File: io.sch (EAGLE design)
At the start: 34 parts, among them J1 SJ-3523-SMT-TR, Q1 MMBT2222A-7-FSOT-23_DIO-M, Q2 2SCR574D3TL1TRANS_2SCR573_TO-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, U1 MCP1703T-5002E, U3 LM386M-1

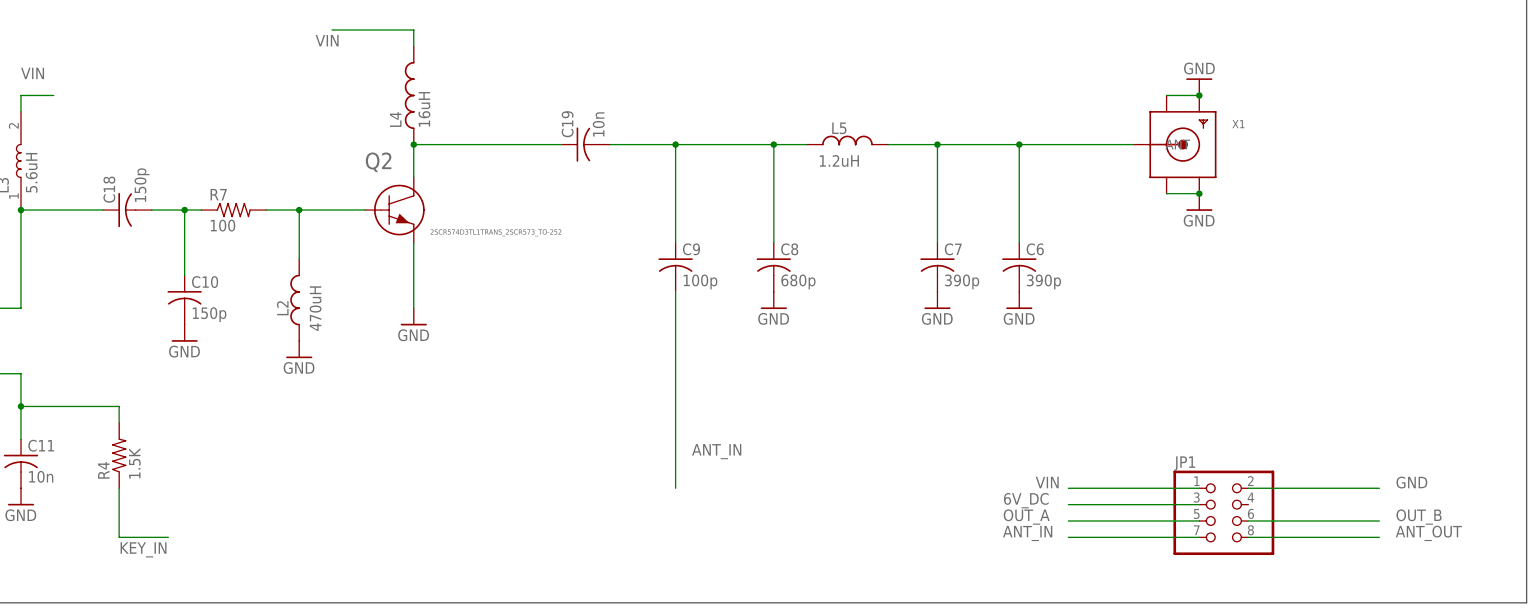
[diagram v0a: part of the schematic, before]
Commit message: v1.2 boards
* corrected C22 as a 33uF (vs 33pF) capacitor with a 1206 footprint
* Q2 emitter is now tied to Q1 emitter and KEY_IN to cut down on self resonance
* Unused pin 4 on JP1 now tied to GND
* All pins on JP1 labelled on top and bottom of each board
* lots more GND vias
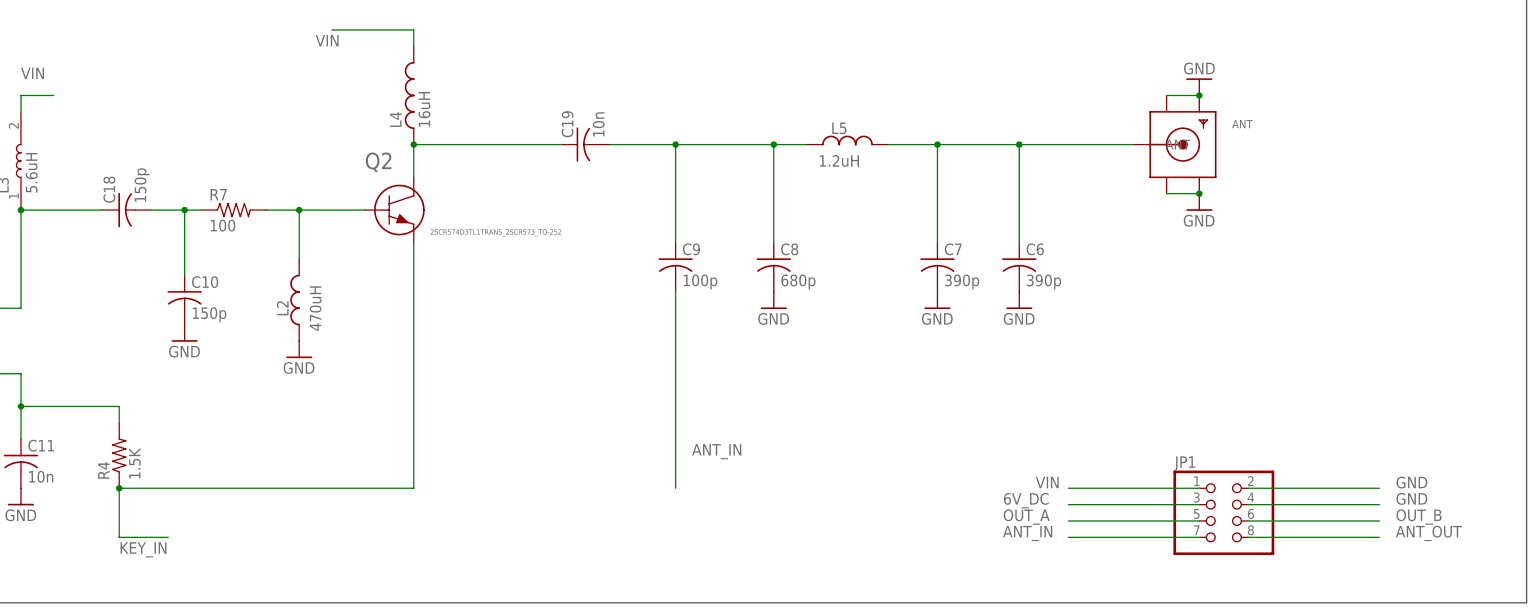
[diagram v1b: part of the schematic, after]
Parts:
- C22: device adafruit:C-USC0805 -> adafruit:C-USC1206
- renumbered X1 to ANT
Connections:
- net GND: now also JP1.4; no longer Q2.3
- net KEY_IN: now also Q2.3
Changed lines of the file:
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@@
 </classes>
 <parts>
-<part name="C22" library="adafruit" library_urn="urn:adsk.eagle:library:420" deviceset="C-US" device="C0805" package3d_urn="urn:adsk.eagle:package:6240337/1" value="33U"/>
+<part name="C22" library="adafruit" library_urn="urn:adsk.eagle:library:420" deviceset="C-US" device="C1206" package3d_urn="urn:adsk.eagle:package:6240335/1" value="33U"/>
 <part name="C1" library="adafruit" library_urn="urn:adsk.eagle:library:420" deviceset="C-US" device="C0805" package3d_urn="urn:adsk.eagle:package:6240337/1" value="0.1U"/>
 <part name="C2" library="adafruit" library_urn="urn:adsk.eagle:library:420" deviceset="C-US" device="C0805" package3d_urn="urn:adsk.eagle:package:6240337/1" value="10n"/>
@@
 <part name="R7" library="adafruit" library_urn="urn:adsk.eagle:library:420" deviceset="R-US_" device="M0805" package3d_urn="urn:adsk.eagle:package:6240587/1" value="100"/>
 <part name="GND21" library="supply1" library_urn="urn:adsk.eagle:library:371" deviceset="GND" device=""/>
-<part name="GND22" library="supply1" library_urn="urn:adsk.eagle:library:371" deviceset="GND" device=""/>
 <part name="GND23" library="supply1" library_urn="urn:adsk.eagle:library:371" deviceset="GND" device=""/>
 <part name="GND24" library="supply1" library_urn="urn:adsk.eagle:library:371" deviceset="GND" device=""/>
@@
 <part name="L2" library="zort2" deviceset="L" device="CHIP-1008(2520-METRIC)" package3d_urn="urn:adsk.eagle:package:16378469/1" technology="_" value="470uH"/>
 <part name="J1" library="SJ-3523-SMT-TR" deviceset="SJ-3523-SMT-TR" device=""/>
-<part name="X1" library="zort2" deviceset="SMACONNECTOR" device="_EDGE" package3d_urn="urn:adsk.eagle:package:6240945/1"/>
+<part name="ANT" library="zort2" deviceset="SMACONNECTOR" device="_EDGE" package3d_urn="urn:adsk.eagle:package:6240945/1"/>
 <part name="Q1" library="zort2" deviceset="MMBT2222A-7-F" device="SOT-23_DIO-M"/>
 </parts>
@@
 <attribute name="VALUE" x="22.86" y="-25.4" size="1.778" layer="96"/>
 </instance>
-<instance part="GND22" gate="1" x="43.18" y="-17.78" smashed="yes">
-<attribute name="VALUE" x="40.64" y="-20.32" size="1.778" layer="96"/>
-</instance>
 <instance part="GND23" gate="1" x="165.1" y="0" smashed="yes">
 <attribute name="VALUE" x="162.56" y="-2.54" size="1.778" layer="96"/>
@@
 <attribute name="NAME" x="185.440409375" y="73.002040625" size="2.201440625" layer="95" rot="R180"/>
 </instance>
-<instance part="X1" gate="G$1" x="162.56" y="10.16" smashed="yes">
+<instance part="ANT" gate="G$1" x="162.56" y="10.16" smashed="yes">
 <attribute name="NAME" x="170.18" y="12.7" size="1.27" layer="95"/>
 <attribute name="VALUE" x="170.18" y="10.16" size="1.27" layer="95"/>
@@
 </segment>
 <segment>
-<pinref part="GND22" gate="1" pin="GND"/>
-<wire x1="43.18" y1="-5.08" x2="43.18" y2="-15.24" width="0.1524" layer="91"/>
-<pinref part="Q2" gate="A" pin="3"/>
-</segment>
-<segment>
 <pinref part="GND23" gate="1" pin="GND"/>
-<pinref part="X1" gate="G$1" pin="GND4"/>
+<pinref part="ANT" gate="G$1" pin="GND4"/>
 <junction x="165.1" y="2.54"/>
 </segment>
 <segment>
 <pinref part="GND24" gate="1" pin="GND"/>
-<pinref part="X1" gate="G$1" pin="GND2"/>
+<pinref part="ANT" gate="G$1" pin="GND2"/>
 <junction x="165.1" y="17.78"/>
 </segment>
@@
 <pinref part="GND21" gate="1" pin="GND"/>
 <pinref part="L2" gate="G$1" pin="1"/>
+</segment>
+<segment>
+<pinref part="JP1" gate="A" pin="4"/>
+<wire x1="172.72" y1="-45.72" x2="193.04" y2="-45.72" width="0.1524" layer="91"/>
+<label x="195.58" y="-45.72" size="1.778" layer="95"/>
 </segment>
 </net>
@@
 </segment>
 </net>
-<net name="KEY_IN" class="0">
+<net name="KEY_IN" class="1">
 <segment>
 <label x="154.94" y="73.66" size="1.778" layer="95" rot="R270"/>
@@
 <label x="-2.54" y="-53.34" size="1.778" layer="95"/>
 <wire x1="-2.54" y1="-50.8" x2="5.08" y2="-50.8" width="0.1524" layer="91"/>
+<pinref part="Q2" gate="A" pin="3"/>
+<wire x1="-2.54" y1="-43.18" x2="43.18" y2="-43.18" width="0.1524" layer="91"/>
+<wire x1="43.18" y1="-43.18" x2="43.18" y2="-5.08" width="0.1524" layer="91"/>
+<junction x="-2.54" y="-43.18"/>
 </segment>
 </net>
@@
 </segment>
 </net>
-<net name="N$19" class="0">
+<net name="N$19" class="1">
 <segment>
 <pinref part="C12" gate="G$1" pin="2"/>
@@
 </segment>
 </net>
-<net name="N$20" class="0">
+<net name="N$20" class="1">
 <segment>
 <pinref part="C11" gate="G$1" pin="1"/>
@@
 <junction x="137.16" y="10.16"/>
 <pinref part="L5" gate="G$1" pin="2"/>
-<pinref part="X1" gate="G$1" pin="ANT"/>
+<pinref part="ANT" gate="G$1" pin="ANT"/>
 </segment>
 </net>
@@
 <segment>
 <wire x1="160.02" y1="2.54" x2="165.0238" y2="2.54" width="0.1524" layer="91"/>
-<pinref part="X1" gate="G$1" pin="GND3"/>
+<pinref part="ANT" gate="G$1" pin="GND3"/>
 </segment>
 </net>
@@
 <segment>
 <wire x1="160.02" y1="17.78" x2="165.0238" y2="17.78" width="0.1524" layer="91"/>
-<pinref part="X1" gate="G$1" pin="GND1"/>
-</segment>
-</net>
+<pinref part="ANT" gate="G$1" pin="GND1"/>
+</segment>
+</net>

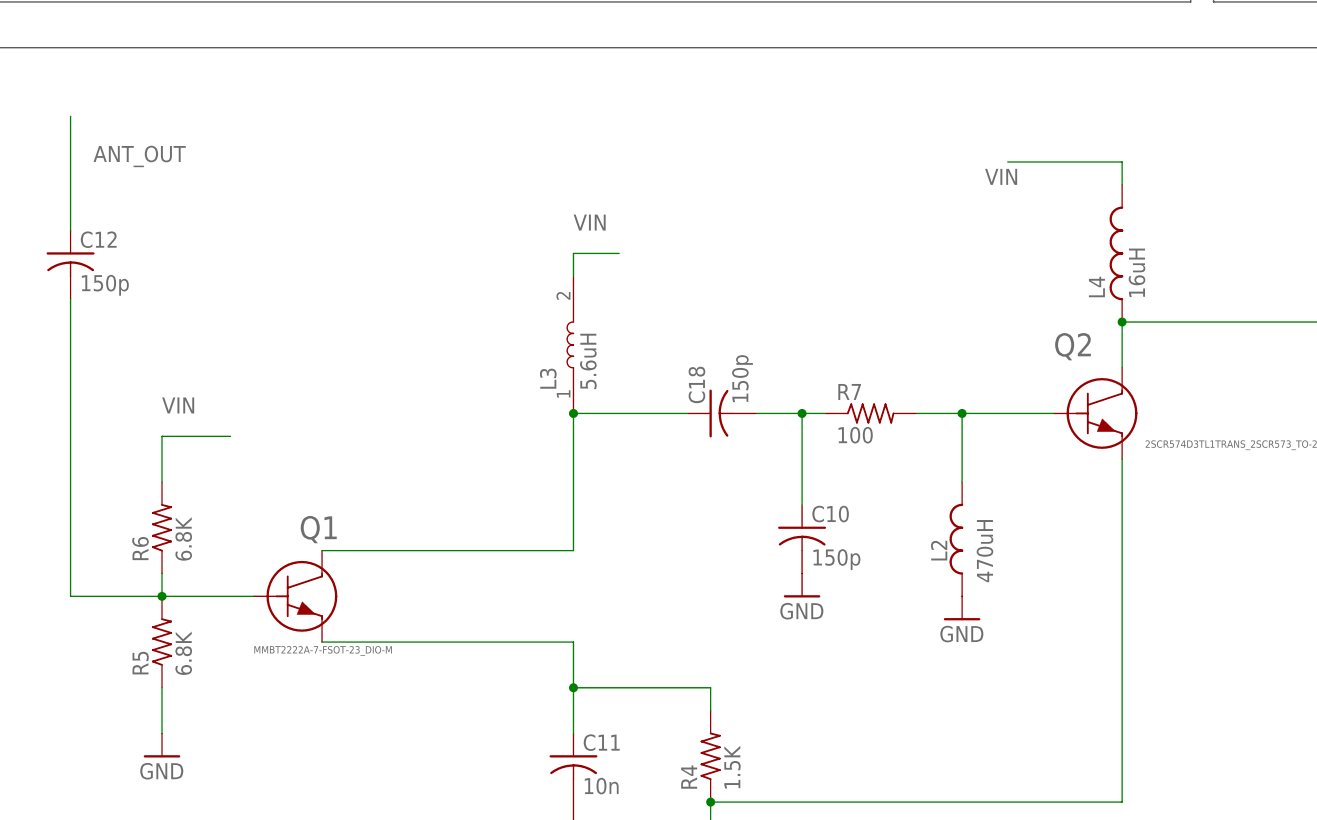
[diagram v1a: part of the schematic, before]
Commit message: v1.2 updated inductors
* updated L3 to a 650mA capable 5.6uH flat package
* updated L4 to a 3A capable 15uH flat package... 16uH are difficult to come by
* general board cleanup for readability
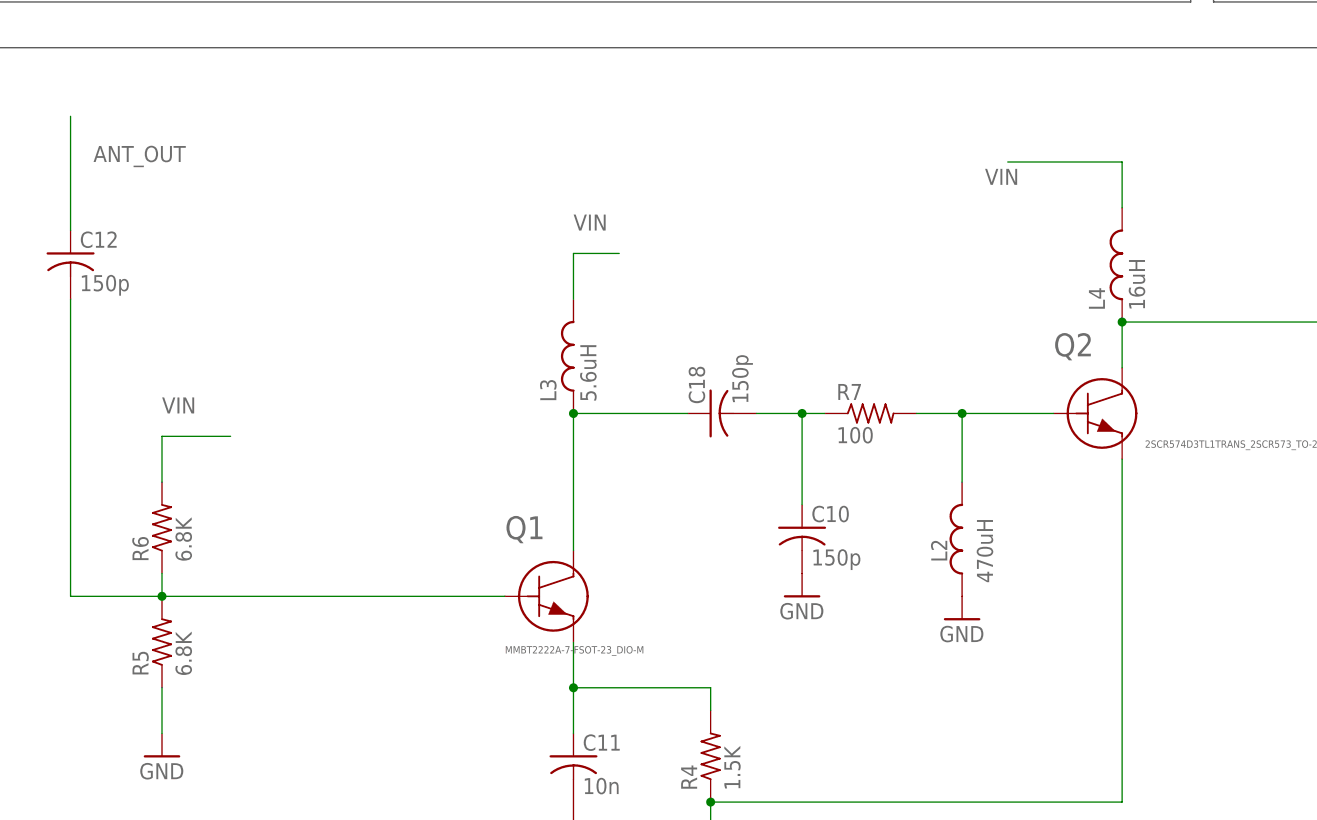
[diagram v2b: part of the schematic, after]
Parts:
- L3: device MLF2012E5R6KT000:MLF2012E5R6KT000 -> zort2:SRP3012C-5R6M
- L4: device LQW18AN16NG8ZD:LQW18AN16NG8ZD -> zort2:ASPI-0630LR
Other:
- moved on the sheet: Q1
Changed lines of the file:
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@@
 <part name="GND19" library="supply1" library_urn="urn:adsk.eagle:library:371" deviceset="GND" device=""/>
 <part name="GND20" library="supply1" library_urn="urn:adsk.eagle:library:371" deviceset="GND" device=""/>
-<part name="L3" library="MLF2012E5R6KT000" deviceset="MLF2012E5R6KT000" device="" value="5.6uH"/>
+<part name="L3" library="zort2" deviceset="SRP3012C-5R6M" device="" value="5.6uH"/>
 <part name="R7" library="adafruit" library_urn="urn:adsk.eagle:library:420" deviceset="R-US_" device="M0805" package3d_urn="urn:adsk.eagle:package:6240587/1" value="100"/>
 <part name="GND21" library="supply1" library_urn="urn:adsk.eagle:library:371" deviceset="GND" device=""/>
@@
 <part name="JP1" library="adafruit" library_urn="urn:adsk.eagle:library:420" deviceset="PINHD-2X4" device="" package3d_urn="urn:adsk.eagle:package:6240893/1"/>
 <part name="L5" library="Inductor" library_urn="urn:adsk.eagle:library:16378440" deviceset="L" device="CHIP-0805(2012-METRIC)" package3d_urn="urn:adsk.eagle:package:16378480/1" technology="_" value="1.2uH"/>
-<part name="L4" library="LQW18AN16NG8ZD" deviceset="LQW18AN16NG8ZD" device="" value="16uH"/>
+<part name="L4" library="zort2" deviceset="ASPI-0630LR" device="" value="16uH"/>
 <part name="U$1" library="zort2" deviceset="9V_968" device="9V_968_SMD"/>
 <part name="Q2" library="zort2" deviceset="2SCR574D3TL1" device="TRANS_2SCR573_TO-252"/>
@@
 <attribute name="VALUE" x="134.62" y="-17.78" size="1.778" layer="96"/>
 </instance>
-<instance part="L3" gate="G$1" x="-17.78" y="7.62" smashed="yes" rot="R90">
-<attribute name="NAME" x="-19.68818125" y="2.53153125" size="1.780959375" layer="95" rot="R90"/>
-<attribute name="VALUE" x="-15.23728125" y="2.534559375" size="1.779909375" layer="96" rot="R90"/>
+<instance part="L3" gate="G$1" x="-17.78" y="6.35" smashed="yes" rot="R90">
+<attribute name="NAME" x="-19.68818125" y="1.26153125" size="1.780959375" layer="95" rot="R90"/>
+<attribute name="VALUE" x="-15.23728125" y="1.264559375" size="1.779909375" layer="96" rot="R90"/>
 </instance>
 <instance part="R7" gate="G$1" x="15.24" y="0" smashed="yes">
@@
 <attribute name="VALUE" x="109.22" y="7.62" size="1.778" layer="96" align="center"/>
 </instance>
-<instance part="L4" gate="G$1" x="43.18" y="17.78" smashed="yes" rot="R90">
-<attribute name="NAME" x="41.27181875" y="12.69153125" size="1.780959375" layer="95" rot="R90"/>
-<attribute name="VALUE" x="45.72271875" y="12.694559375" size="1.779909375" layer="96" rot="R90"/>
+<instance part="L4" gate="G$1" x="43.18" y="16.51" smashed="yes" rot="R90">
+<attribute name="NAME" x="41.27181875" y="11.42153125" size="1.780959375" layer="95" rot="R90"/>
+<attribute name="VALUE" x="45.72271875" y="11.424559375" size="1.779909375" layer="96" rot="R90"/>
 </instance>
 <instance part="U$1" gate="G$1" x="-78.74" y="88.9" smashed="yes"/>
@@
 <attribute name="VALUE" x="170.18" y="10.16" size="1.27" layer="95"/>
 </instance>
-<instance part="Q1" gate="G$1" x="-48.26" y="-20.32" smashed="yes">
-<attribute name="NAME" x="-48.26" y="-13.97" size="2.54" layer="95" ratio="10" rot="SR0"/>
-<attribute name="VALUE" x="-53.34" y="-26.67" size="0.8128" layer="96" ratio="10" rot="SR0"/>
+<instance part="Q1" gate="G$1" x="-20.32" y="-20.32" smashed="yes">
+<attribute name="NAME" x="-25.4" y="-13.97" size="2.54" layer="95" ratio="10" rot="SR0"/>
+<attribute name="VALUE" x="-25.4" y="-26.67" size="0.8128" layer="96" ratio="10" rot="SR0"/>
 </instance>
 </instances>
@@
 <segment>
 <pinref part="L3" gate="G$1" pin="2"/>
-<wire x1="-17.78" y1="15.24" x2="-17.78" y2="17.78" width="0.1524" layer="91"/>
+<wire x1="-17.78" y1="12.7" x2="-17.78" y2="17.78" width="0.1524" layer="91"/>
 <wire x1="-17.78" y1="17.78" x2="-12.7" y2="17.78" width="0.1524" layer="91"/>
 <label x="-17.78" y="20.32" size="1.778" layer="95"/>
 </segment>
 <segment>
-<wire x1="43.18" y1="25.4" x2="43.18" y2="27.94" width="0.1524" layer="91"/>
+<wire x1="43.18" y1="22.86" x2="43.18" y2="27.94" width="0.1524" layer="91"/>
 <wire x1="43.18" y1="27.94" x2="30.48" y2="27.94" width="0.1524" layer="91"/>
 <label x="27.94" y="25.4" size="1.778" layer="95"/>
@@
 <wire x1="-73.66" y1="-20.32" x2="-63.5" y2="-20.32" width="0.1524" layer="91"/>
 <pinref part="R5" gate="G$1" pin="2"/>
-<wire x1="-63.5" y1="-20.32" x2="-53.34" y2="-20.32" width="0.1524" layer="91"/>
+<wire x1="-63.5" y1="-20.32" x2="-25.4" y2="-20.32" width="0.1524" layer="91"/>
 <junction x="-63.5" y="-20.32"/>
 <pinref part="R6" gate="G$1" pin="1"/>
@@
 <wire x1="-2.54" y1="-30.48" x2="-2.54" y2="-33.02" width="0.1524" layer="91"/>
 <pinref part="Q1" gate="G$1" pin="3"/>
-<wire x1="-45.72" y1="-25.4" x2="-17.78" y2="-25.4" width="0.1524" layer="91"/>
 <wire x1="-17.78" y1="-25.4" x2="-17.78" y2="-30.48" width="0.1524" layer="91"/>
 </segment>
 </net>
-<net name="N$21" class="0">
+<net name="N$21" class="1">
 <segment>
 <pinref part="L3" gate="G$1" pin="1"/>
@@
 <junction x="-17.78" y="0"/>
 <pinref part="Q1" gate="G$1" pin="2"/>
-<wire x1="-45.72" y1="-15.24" x2="-17.78" y2="-15.24" width="0.1524" layer="91"/>
-</segment>
-</net>
-<net name="N$22" class="0">
+</segment>
+</net>
+<net name="N$22" class="1">
 <segment>
 <pinref part="C18" gate="G$1" pin="2"/>
